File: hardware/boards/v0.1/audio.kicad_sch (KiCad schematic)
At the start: 47 parts, among them J4 SPKR_L, J5 SPKR_R, J8 LINE_OUT, J9 LINE_IN, U24 MIC, U28 TS5A23159RSE, U29 NAU88C22YG, U30 SI4704-D60-GM, U34 SI4710-B30-GMR, Y3 ASVK-32.768KHZ-LJ-T, Y5 ASVK-32.768KHZ-LJ-T

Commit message: fix: more ERC cleanup
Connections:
- now unconnected: U34.1 (NC), U34.2 (NC), U34.20 (NC)
- no-connect marks 6 -> 7
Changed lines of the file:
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@@
+	)
+	(junction
+		(at 240.03 153.67)
+		(diameter 0)
+		(color 0 0 0 0)
 	)
 	(junction
@@
 	)
 	(junction
+		(at 243.84 153.67)
+		(diameter 0)
+		(color 0 0 0 0)
+	)
+	(junction
 		(at 120.65 90.17)
 		(diameter 0)
@@
 	)
 	(junction
-		(at 224.79 152.4)
-		(diameter 0)
-		(color 0 0 0 0)
-	)
-	(junction
 		(at 208.28 138.43)
 		(diameter 0)
@@
 	)
 	(junction
+		(at 224.79 153.67)
+		(diameter 0)
+		(color 0 0 0 0)
+	)
+	(junction
 		(at 246.38 80.01)
 		(diameter 0)
@@
 	)
 	(junction
-		(at 256.54 152.4)
-		(diameter 0)
-		(color 0 0 0 0)
-	)
-	(junction
 		(at 80.01 24.13)
 		(diameter 0)
@@
 	)
 	(junction
+		(at 256.54 153.67)
+		(diameter 0)
+		(color 0 0 0 0)
+	)
+	(junction
 		(at 107.95 128.27)
 		(diameter 0)
@@
 	)
 	(junction
-		(at 243.84 152.4)
-		(diameter 0)
-		(color 0 0 0 0)
-	)
-	(junction
 		(at 224.79 20.32)
-		(diameter 0)
-		(color 0 0 0 0)
-	)
-	(junction
-		(at 240.03 152.4)
 		(diameter 0)
 		(color 0 0 0 0)
@@
 	(no_connect
 		(at 240.03 125.73)
+	)
+	(no_connect
+		(at 59.69 76.2)
 	)
 	(no_connect
@@
 	(wire
 		(pts
-			(xy 208.28 152.4) (xy 224.79 152.4)
+			(xy 208.28 153.67) (xy 224.79 153.67)
 		)
 		(stroke
@@
 		(pts
 			(xy 241.3 73.66) (xy 242.57 73.66)
-		)
-		(stroke
-			(width 0)
-			(type default)
-		)
-	)
-	(wire
-		(pts
-			(xy 243.84 151.13) (xy 243.84 152.4)
 		)
 		(stroke
@@
 	(wire
 		(pts
+			(xy 256.54 148.59) (xy 256.54 153.67)
+		)
+		(stroke
+			(width 0)
+			(type default)
+		)
+	)
+	(wire
+		(pts
 			(xy 198.12 69.85) (xy 198.12 71.12)
 		)
@@
 	(wire
 		(pts
+			(xy 224.79 153.67) (xy 224.79 157.48)
+		)
+		(stroke
+			(width 0)
+			(type default)
+		)
+	)
+	(wire
+		(pts
 			(xy 144.78 191.77) (xy 147.32 191.77)
 		)
@@
 	(wire
 		(pts
-			(xy 224.79 152.4) (xy 224.79 157.48)
-		)
-		(stroke
-			(width 0)
-			(type default)
-		)
-	)
-	(wire
-		(pts
 			(xy 81.28 128.27) (xy 83.82 128.27)
 		)
@@
 	(wire
 		(pts
-			(xy 256.54 152.4) (xy 269.24 152.4)
+			(xy 256.54 153.67) (xy 269.24 153.67)
 		)
 		(stroke
@@
 	(wire
 		(pts
-			(xy 224.79 151.13) (xy 224.79 152.4)
-		)
-		(stroke
-			(width 0)
-			(type default)
-		)
-	)
-	(wire
-		(pts
 			(xy 137.16 170.18) (xy 137.16 181.61)
 		)
@@
 	(wire
 		(pts
-			(xy 240.03 146.05) (xy 240.03 152.4)
-		)
-		(stroke
-			(width 0)
-			(type default)
-		)
-	)
-	(wire
-		(pts
-			(xy 240.03 152.4) (xy 243.84 152.4)
+			(xy 240.03 153.67) (xy 243.84 153.67)
 		)
 		(stroke
@@
 	(wire
 		(pts
-			(xy 240.03 152.4) (xy 224.79 152.4)
+			(xy 240.03 153.67) (xy 224.79 153.67)
 		)
 		(stroke
@@
 	(wire
 		(pts
-			(xy 269.24 152.4) (xy 269.24 151.13)
-		)
-		(stroke
-			(width 0)
-			(type default)
-		)
-	)
-	(wire
-		(pts
-			(xy 208.28 138.43) (xy 208.28 152.4)
+			(xy 269.24 153.67) (xy 269.24 151.13)
+		)
+		(stroke
+			(width 0)
+			(type default)
+		)
+	)
+	(wire
+		(pts
+			(xy 208.28 138.43) (xy 208.28 153.67)
 		)
 		(stroke
@@
 		(pts
 			(xy 144.78 158.75) (xy 147.32 158.75)
+		)
+		(stroke
+			(width 0)
+			(type default)
+		)
+	)
+	(wire
+		(pts
+			(xy 240.03 146.05) (xy 240.03 153.67)
 		)
 		(stroke
@@
 	(wire
 		(pts
+			(xy 243.84 151.13) (xy 243.84 153.67)
+		)
+		(stroke
+			(width 0)
+			(type default)
+		)
+	)
+	(wire
+		(pts
+			(xy 224.79 151.13) (xy 224.79 153.67)
+		)
+		(stroke
+			(width 0)
+			(type default)
+		)
+	)
+	(wire
+		(pts
 			(xy 115.57 67.31) (xy 123.19 67.31)
 		)
@@
 	(wire
 		(pts
-			(xy 256.54 148.59) (xy 256.54 152.4)
-		)
-		(stroke
-			(width 0)
-			(type default)
-		)
-	)
-	(wire
-		(pts
 			(xy 123.19 82.55) (xy 120.65 82.55)
 		)
@@
 	(wire
 		(pts
-			(xy 243.84 152.4) (xy 256.54 152.4)
-		)
-		(stroke
+			(xy 243.84 153.67) (xy 256.54 153.67)
+		)
+		(stroke

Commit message: feat: more DRC cleanup
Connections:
- net +3.3V: now also U30.5 (~{RST}), U34.5 (~{RST})
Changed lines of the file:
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@@
 	(wire
 		(pts
+			(xy 207.01 110.49) (xy 209.55 110.49)
+		)
+		(stroke
+			(width 0)
+			(type default)
+		)
+	)
+	(wire
+		(pts
 			(xy 224.79 153.67) (xy 224.79 157.48)
 		)
@@
 	(wire
 		(pts
+			(xy 207.01 107.95) (xy 207.01 110.49)
+		)
+		(stroke
+			(width 0)
+			(type default)
+		)
+	)
+	(wire
+		(pts
 			(xy 57.15 115.57) (xy 57.15 116.84)
 		)
@@
 	(wire
 		(pts
+			(xy 208.28 40.64) (xy 210.82 40.64)
+		)
+		(stroke
+			(width 0)
+			(type default)
+		)
+	)
+	(wire
+		(pts
 			(xy 240.03 140.97) (xy 243.84 140.97)
 		)
@@
 	(wire
 		(pts
+			(xy 208.28 38.1) (xy 208.28 40.64)
+		)
+		(stroke
+			(width 0)
+			(type default)
+		)
+	)
+	(wire
+		(pts
 			(xy 123.19 82.55) (xy 120.65 82.55)
 		)
@@
 	(symbol
 		(lib_id "power:+3.3V")
+		(at 208.28 38.1 0)
+		(unit 1)
+		(exclude_from_sim no)
+		(in_bom yes)
+		(on_board yes)
+		(dnp no)
+		(property "Reference" "#PWR083"
+			(at 208.28 41.91 0)
+			(effects
+				(font
+					(size 1.27 1.27)
+				)
+				(hide yes)
+			)
+		)
+		(property "Value" "+3.3V"
+			(at 208.28 33.528 0)
+			(effects
+				(font
+					(size 1.27 1.27)
+				)
+			)
+		)
+		(property "Footprint" ""
+			(at 208.28 38.1 0)
+			(effects
+				(font
+					(size 1.27 1.27)
+				)
+				(hide yes)
+			)
+		)
+		(property "Datasheet" ""
+			(at 208.28 38.1 0)
+			(effects
+				(font
+					(size 1.27 1.27)
+				)
+				(hide yes)
+			)
+		)
+		(property "Description" "Power symbol creates a global label with name \"+3.3V\""
+			(at 208.28 38.1 0)
+			(effects
+				(font
+					(size 1.27 1.27)
+				)
+				(hide yes)
+			)
+		)
+		(pin "1"
+		)
+		(instances
+			(project "pocket_synth"
+				(path "/485383b8-00f4-4405-b270-de249939cff4/ac7a2cd5-8a17-4132-a50f-a1edfbc58e6d"
+					(reference "#PWR083")
+					(unit 1)
+				)
+			)
+		)
+	)
+	(symbol
+		(lib_id "power:+3.3V")
 		(at 259.08 57.15 0)
 		(unit 1)
@@
 					(unit 1)
 				)
+			)
+		)
+	)
+	(symbol
+		(lib_id "power:+3.3V")
+		(at 207.01 107.95 0)
+		(unit 1)
+		(exclude_from_sim no)
+		(in_bom yes)
+		(on_board yes)
+		(dnp no)
+		(property "Reference" "#PWR084"
+			(at 207.01 111.76 0)
+			(effects
+				(font
+					(size 1.27 1.27)
+				)
+				(hide yes)
+			)
+		)
+		(property "Value" "+3.3V"
+			(at 207.01 103.378 0)
+			(effects
+				(font
+					(size 1.27 1.27)
+				)
+			)
+		)
+		(property "Footprint" ""
+			(at 207.01 107.95 0)
+			(effects
+				(font
+					(size 1.27 1.27)
+				)
+				(hide yes)
+			)
+		)
+		(property "Datasheet" ""
+			(at 207.01 107.95 0)
+			(effects
+				(font
+					(size 1.27 1.27)
+				)
+				(hide yes)
+			)
+		)
+		(property "Description" "Power symbol creates a global label with name \"+3.3V\""
+			(at 207.01 107.95 0)
+			(effects
+				(font
+					(size 1.27 1.27)
+				)
+				(hide yes)
+			)
+		)
+		(pin "1"
+		)
+		(instances
+			(project "pocket_synth"
+				(path "/485383b8-00f4-4405-b270-de249939cff4/ac7a2cd5-8a17-4132-a50f-a1edfbc58e6d"
+					(reference "#PWR084")
+					(unit 1)
+				)

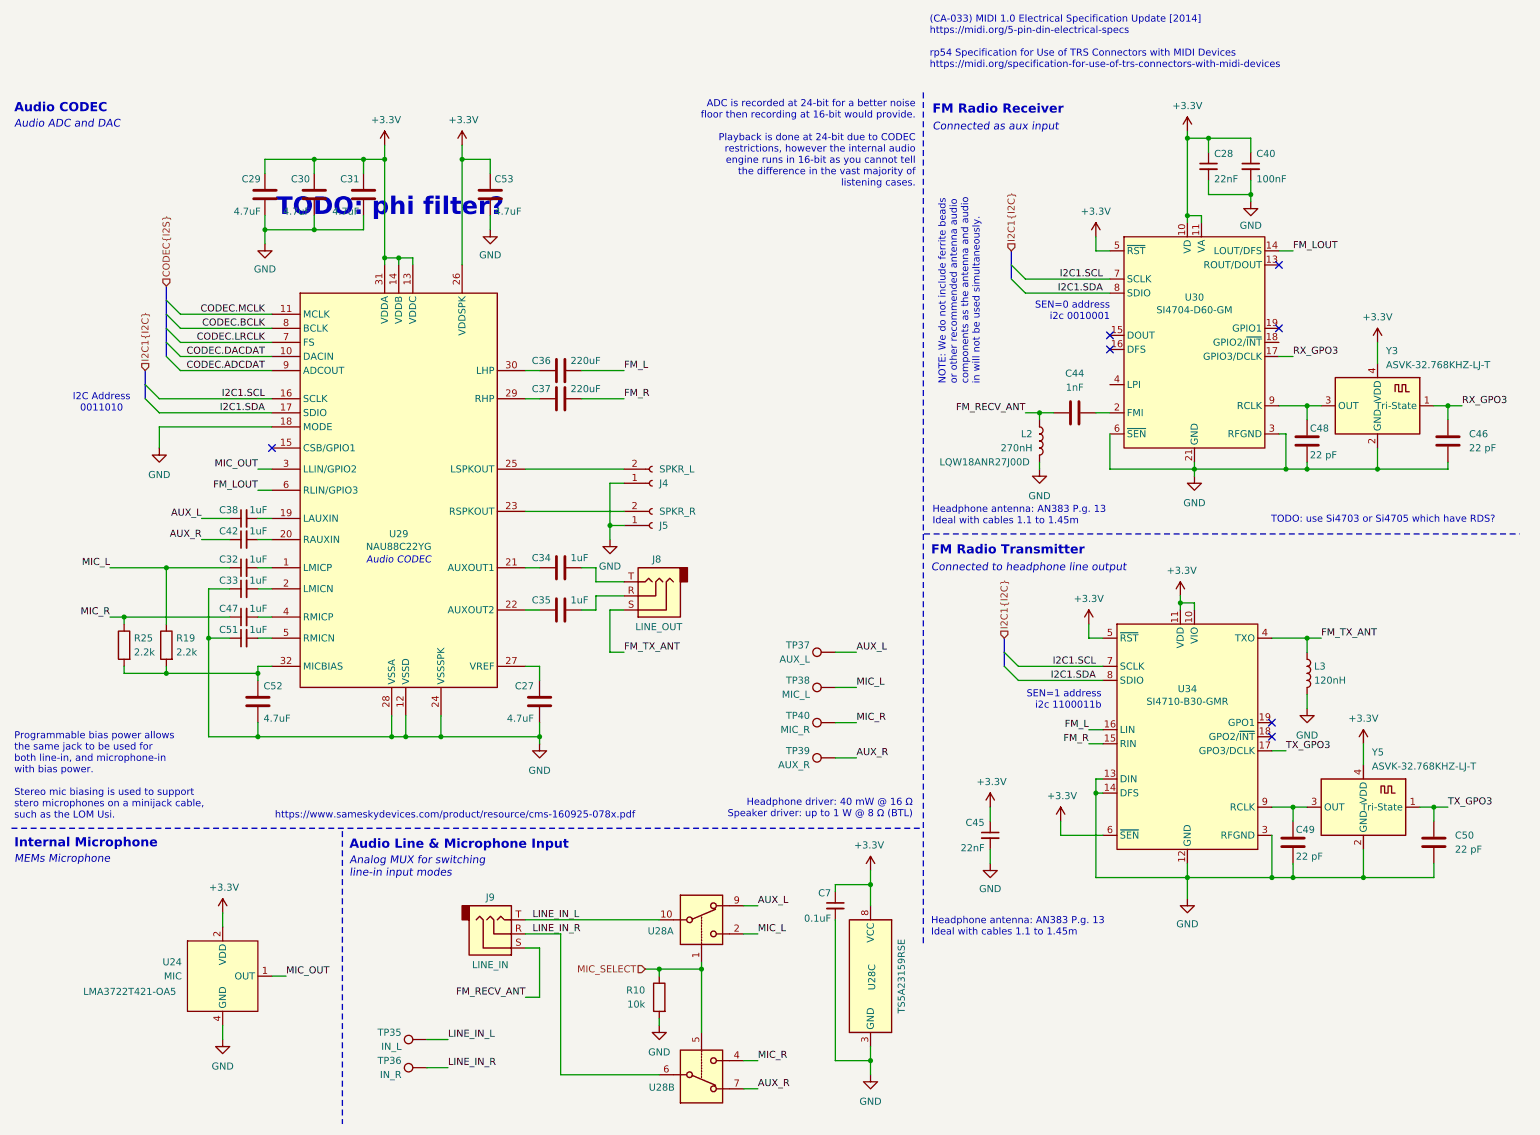
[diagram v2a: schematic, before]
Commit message: feat: switch FM transmitter to I2S
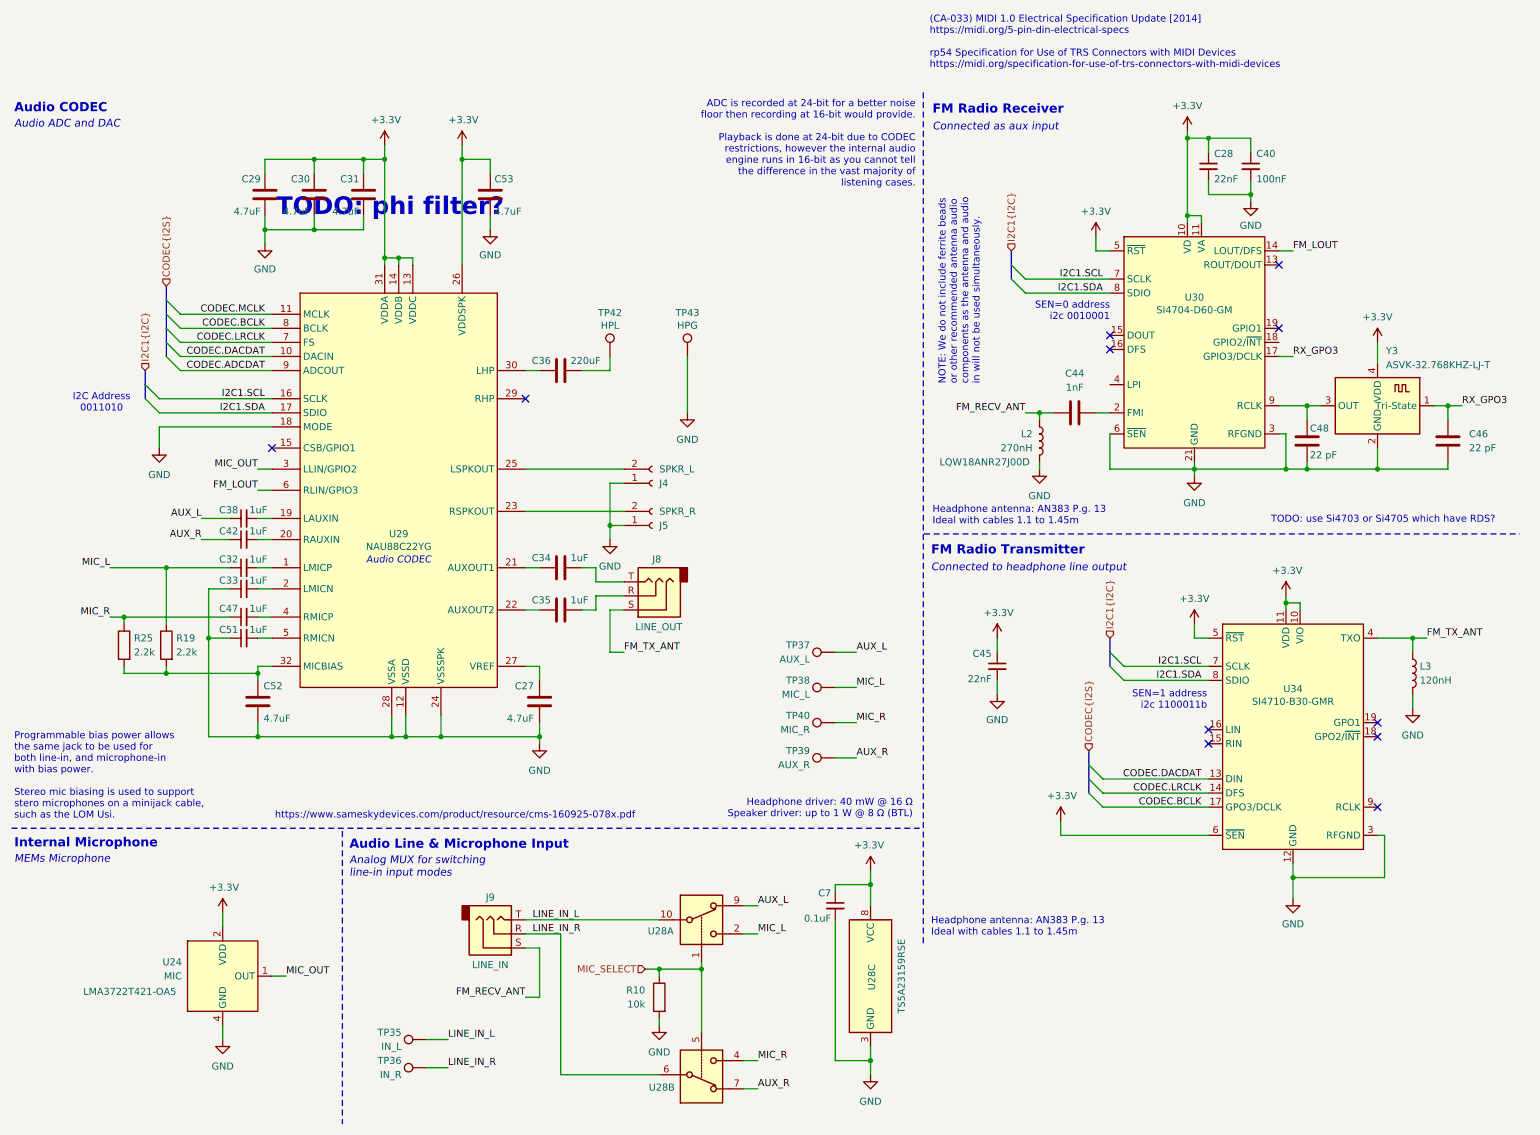
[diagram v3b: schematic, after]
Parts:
- removed C37: 220uF, Capacitor_SMD:C_0603_1608Metric, symbol Device:C
- removed C49, C50: 22 pF, Capacitor_SMD:C_0603_1608Metric, symbol Device:C
- removed Y5: ASVK-32.768KHZ-LJ-T, Oscillator:Oscillator_SMD_Abracon_ASCO-4Pin_1.6x1.2mm, symbol Oscillator:ASCO
- added TP42: HPL, TestPoint:TestPoint_Pad_D2.0mm, symbol Connector:TestPoint
- added TP43: HPG, TestPoint:TestPoint_Pad_D2.0mm, symbol Connector:TestPoint
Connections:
- net TX_GPO3 is gone; now on net CODEC.BCLK: U34.17 (GPO3/DCLK)
- net CODEC.DACDAT: now also U34.13 (DIN)
- net CODEC.LRCLK: now also U34.14 (DFS)
- net GND: now also TP43.1; no longer U34.13 (DIN), U34.14 (DFS)
- net FM_L: no longer names the net of U34.16 (LIN)
- net FM_L: no longer C36.2
- net FM_R: no longer names the net of U34.15 (RIN)
- new net: C36.2, TP42.1
- no-connect marks 7 -> 11
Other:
- moved on the sheet: C45, L3, U34
